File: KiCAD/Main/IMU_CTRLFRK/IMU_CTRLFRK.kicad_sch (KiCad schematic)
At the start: 12 parts, among them U1 BNO085, U2 BME280, U3 VCNL4040M3OE

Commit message: Continue integrating
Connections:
- net +3V3: now also U1.6 (PS0/WAKE)
- net BNO_CLKSELD: now reaches U1.10 (CLKSEL0)
- net BNO_RST: now reaches U1.11 (~{RST})
- net BNO_INT: now reaches U1.14 (~{H_INT})
- net BNO_MOSI: now reaches U1.17 (SA0/H_MOSI)
- net BNO_CS: now reaches U1.18 (~{H_CS})
- net BNO_SCK: now reaches U1.19 (H_SCL/SCK/RX)
- net BNO_MISO: now reaches U1.20 (H_SDA/H_MISO/TX)
- net BNO_BOOT: now reaches R3.2, U1.4 (~{BOOT})
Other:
- note removed: "Microprocessor Interface"
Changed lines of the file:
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@@
 	(generator_version "9.0")
 	(paper "A4")
-	(text "Microprocessor Interface"
-		(exclude_from_sim no)
-		(at 53.086 107.95 90)
-		(effects
-			(font
-				(size 1.905 1.905)
-			)
-		)
-	)
 	(junction
 		(at 218.44 58.42)
@@
 	)
 	(junction
+		(at 116.84 139.7)
+		(diameter 0)
+		(color 0 0 0 0)
+	)
+	(junction
 		(at 213.36 119.38)
 		(diameter 0)
@@
 	(wire
 		(pts
-			(xy 119.38 142.24) (xy 96.52 142.24)
-		)
-		(stroke
-			(width 0)
-			(type default)
-		)
-	)
-	(wire
-		(pts
 			(xy 180.34 121.92) (xy 184.15 121.92)
 		)
@@
 	(wire
 		(pts
-			(xy 119.38 139.7) (xy 114.3 139.7)
-		)
-		(stroke
-			(width 0)
-			(type default)
-		)
-	)
-	(wire
-		(pts
 			(xy 180.34 127) (xy 233.68 127)
 		)
@@
 	(wire
 		(pts
-			(xy 114.3 109.22) (xy 184.15 109.22)
+			(xy 116.84 109.22) (xy 184.15 109.22)
 		)
 		(stroke
@@
 	(wire
 		(pts
-			(xy 114.3 139.7) (xy 114.3 109.22)
+			(xy 116.84 139.7) (xy 116.84 109.22)
 		)
 		(stroke
@@
 	(wire
 		(pts
+			(xy 116.84 139.7) (xy 116.84 142.24)
+		)
+		(stroke
+			(width 0)
+			(type default)
+		)
+	)
+	(wire
+		(pts
 			(xy 57.15 116.84) (xy 93.98 116.84)
 		)
@@
 	(wire
 		(pts
-			(xy 96.52 142.24) (xy 96.52 114.3)
-		)
-		(stroke
-			(width 0)
-			(type default)
-		)
-	)
-	(wire
-		(pts
 			(xy 109.22 129.54) (xy 109.22 101.6)
 		)
@@
 	(wire
 		(pts
+			(xy 116.84 142.24) (xy 119.38 142.24)
+		)
+		(stroke
+			(width 0)
+			(type default)
+		)
+	)
+	(wire
+		(pts
 			(xy 212.09 26.67) (xy 189.23 26.67)
 		)
@@
 	(wire
 		(pts
-			(xy 57.15 114.3) (xy 96.52 114.3)
+			(xy 116.84 139.7) (xy 119.38 139.7)
 		)
 		(stroke
@@
 			(width 0)
 			(type default)
+		)
+	)
+	(hierarchical_label "BNO_CLKSELD"
+		(shape input)
+		(at 57.15 116.84 180)
+		(effects
+			(font
+				(size 1.27 1.27)
+			)
+			(justify right)
+		)
+	)
+	(hierarchical_label "BNO_SCK"
+		(shape input)
+		(at 57.15 104.14 180)
+		(effects
+			(font
+				(size 1.27 1.27)
+			)
+			(justify right)
+		)
+	)
+	(hierarchical_label "BNO_MISO"
+		(shape input)
+		(at 57.15 101.6 180)
+		(effects
+			(font
+				(size 1.27 1.27)
+			)
+			(justify right)
+		)
+	)
+	(hierarchical_label "BNO_MOSI"
+		(shape input)
+		(at 57.15 99.06 180)
+		(effects
+			(font
+				(size 1.27 1.27)
+			)
+			(justify right)
+		)
+	)
+	(hierarchical_label "BNO_CS"
+		(shape input)
+		(at 57.15 119.38 180)
+		(effects
+			(font
+				(size 1.27 1.27)
+			)
+			(justify right)
+		)
+	)
+	(hierarchical_label "BNO_INT"
+		(shape input)
+		(at 57.15 106.68 180)
+		(effects
+			(font
+				(size 1.27 1.27)
+			)
+			(justify right)
+		)
+	)
+	(hierarchical_label "BNO_RST"
+		(shape input)
+		(at 57.15 96.52 180)
+		(effects
+			(font
+				(size 1.27 1.27)
+			)
+			(justify right)
+		)
+	)
+	(hierarchical_label "BNO_BOOT"
+		(shape input)
+		(at 57.15 109.22 180)
+		(effects
+			(font
+				(size 1.27 1.27)
+			)
+			(justify right)
 		)
 	)
@@
 				)
 			)
+			(project "IMU_CTRLFRK"
+				(path "/bbb10697-a5dd-43b8-9c6f-4c5919cf3463/a6ed620d-2e9d-447a-9d61-86e453a954d4"
+					(reference "C4")
+					(unit 1)
+				)
+			)
 		)
 	)
@@
 				)
 			)
+			(project "IMU_CTRLFRK"
+				(path "/bbb10697-a5dd-43b8-9c6f-4c5919cf3463/a6ed620d-2e9d-447a-9d61-86e453a954d4"
+					(reference "U1")
+					(unit 1)
+				)
+			)
 		)
 	)
@@
 				)
 			)
+			(project "IMU_CTRLFRK"
+				(path "/bbb10697-a5dd-43b8-9c6f-4c5919cf3463/a6ed620d-2e9d-447a-9d61-86e453a954d4"
+					(reference "C3")
+					(unit 1)
+				)
+			)
 		)
 	)
@@
 				)
 			)
+			(project "IMU_CTRLFRK"
+				(path "/bbb10697-a5dd-43b8-9c6f-4c5919cf3463/a6ed620d-2e9d-447a-9d61-86e453a954d4"
+					(reference "C1")
+					(unit 1)
+				)
+			)
 		)
 	)
@@
 				)
 			)
+			(project "IMU_CTRLFRK"
+				(path "/bbb10697-a5dd-43b8-9c6f-4c5919cf3463/a6ed620d-2e9d-447a-9d61-86e453a954d4"
+					(reference "R3")
+					(unit 1)
+				)
+			)
 		)
 	)
@@
 				)
 			)
+			(project "IMU_CTRLFRK"
+				(path "/bbb10697-a5dd-43b8-9c6f-4c5919cf3463/a6ed620d-2e9d-447a-9d61-86e453a954d4"
+					(reference "#PWR08")
+					(unit 1)
+				)
+			)
 		)
 	)
@@
 				)
 			)
+			(project "IMU_CTRLFRK"
+				(path "/bbb10697-a5dd-43b8-9c6f-4c5919cf3463/a6ed620d-2e9d-447a-9d61-86e453a954d4"
+					(reference "#PWR06")
+					(unit 1)
+				)
+			)
 		)
 	)
@@
 			(project "IMU_CTRLFRK"
 				(path "/aead792a-4a3a-422e-8f19-9a151b1cac78"
+					(reference "R1")
+					(unit 1)
+				)
+			)
+			(project "IMU_CTRLFRK"
+				(path "/bbb10697-a5dd-43b8-9c6f-4c5919cf3463/a6ed620d-2e9d-447a-9d61-86e453a954d4"
 					(reference "R1")
 					(unit 1)
@@
 				)
 			)
+			(project "IMU_CTRLFRK"
+				(path "/bbb10697-a5dd-43b8-9c6f-4c5919cf3463/a6ed620d-2e9d-447a-9d61-86e453a954d4"
+					(reference "U2")
+					(unit 1)
+				)
+			)
 		)
 	)
@@
 				)
 			)
+			(project "IMU_CTRLFRK"
+				(path "/bbb10697-a5dd-43b8-9c6f-4c5919cf3463/a6ed620d-2e9d-447a-9d61-86e453a954d4"
+					(reference "#PWR011")
+					(unit 1)
+				)
+			)
 		)
 	)
@@
 				)
 			)
+			(project "IMU_CTRLFRK"
+				(path "/bbb10697-a5dd-43b8-9c6f-4c5919cf3463/a6ed620d-2e9d-447a-9d61-86e453a954d4"
+					(reference "#PWR04")
+					(unit 1)
+				)
+			)
 		)
 	)
@@
 				)
 			)
+			(project "IMU_CTRLFRK"
+				(path "/bbb10697-a5dd-43b8-9c6f-4c5919cf3463/a6ed620d-2e9d-447a-9d61-86e453a954d4"
+					(reference "C2")
+					(unit 1)
+				)
+			)
 		)
 	)
@@
 				)
 			)
+			(project "IMU_CTRLFRK"
+				(path "/bbb10697-a5dd-43b8-9c6f-4c5919cf3463/a6ed620d-2e9d-447a-9d61-86e453a954d4"
+					(reference "#PWR03")
+					(unit 1)
+				)
+			)
 		)
 	)
@@
 				)
 			)
+			(project "IMU_CTRLFRK"
+				(path "/bbb10697-a5dd-43b8-9c6f-4c5919cf3463/a6ed620d-2e9d-447a-9d61-86e453a954d4"
+					(reference "C5")
+					(unit 1)
+				)
+			)
 		)
 	)
@@
 				)
 			)
+			(project "IMU_CTRLFRK"
+				(path "/bbb10697-a5dd-43b8-9c6f-4c5919cf3463/a6ed620d-2e9d-447a-9d61-86e453a954d4"
+					(reference "#PWR010")
+					(unit 1)
+				)
+			)
 		)
 	)
@@
 				)
 			)
+			(project "IMU_CTRLFRK"
+				(path "/bbb10697-a5dd-43b8-9c6f-4c5919cf3463/a6ed620d-2e9d-447a-9d61-86e453a954d4"
+					(reference "#PWR05")
+					(unit 1)
+				)
+			)
 		)
 	)
@@
 				)
 			)
+			(project "IMU_CTRLFRK"
+				(path "/bbb10697-a5dd-43b8-9c6f-4c5919cf3463/a6ed620d-2e9d-447a-9d61-86e453a954d4"
+					(reference "#PWR01")
+					(unit 1)
+				)
+			)
 		)
 	)
@@
 				)
 			)
+			(project "IMU_CTRLFRK"
+				(path "/bbb10697-a5dd-43b8-9c6f-4c5919cf3463/a6ed620d-2e9d-447a-9d61-86e453a954d4"
+					(reference "Y1")
+					(unit 1)
+				)
+			)
 		)
 	)
@@
 				)
 			)
+			(project "IMU_CTRLFRK"
+				(path "/bbb10697-a5dd-43b8-9c6f-4c5919cf3463/a6ed620d-2e9d-447a-9d61-86e453a954d4"
+					(reference "#PWR02")
+					(unit 1)
+				)
+			)
 		)
 	)
@@
 				)
 			)
+			(project "IMU_CTRLFRK"
+				(path "/bbb10697-a5dd-43b8-9c6f-4c5919cf3463/a6ed620d-2e9d-447a-9d61-86e453a954d4"
+					(reference "R2")
+					(unit 1)
+				)
+			)
 		)
 	)
@@
 				)
 			)
+			(project "IMU_CTRLFRK"
+				(path "/bbb10697-a5dd-43b8-9c6f-4c5919cf3463/a6ed620d-2e9d-447a-9d61-86e453a954d4"
+					(reference "#PWR07")
+					(unit 1)
+				)
+			)
 		)
 	)
@@
 				)
 			)
+			(project "IMU_CTRLFRK"
+				(path "/bbb10697-a5dd-43b8-9c6f-4c5919cf3463/a6ed620d-2e9d-447a-9d61-86e453a954d4"
+					(reference "#PWR09")
+					(unit 1)
+				)
+			)
 		)
 	)
@@
 				)
 			)
-		)
-	)
-	(sheet_instances
-		(path "/"
-			(page "1")
-		)
-	)
-	(embedded_fonts no)
+			(project "IMU_CTRLFRK"
+				(path "/bbb10697-a5dd-43b8-9c6f-4c5919cf3463/a6ed620d-2e9d-447a-9d61-86e453a954d4"
+					(reference "U3")
+					(unit 1)
+				)
+			)
+		)
+	)
 )

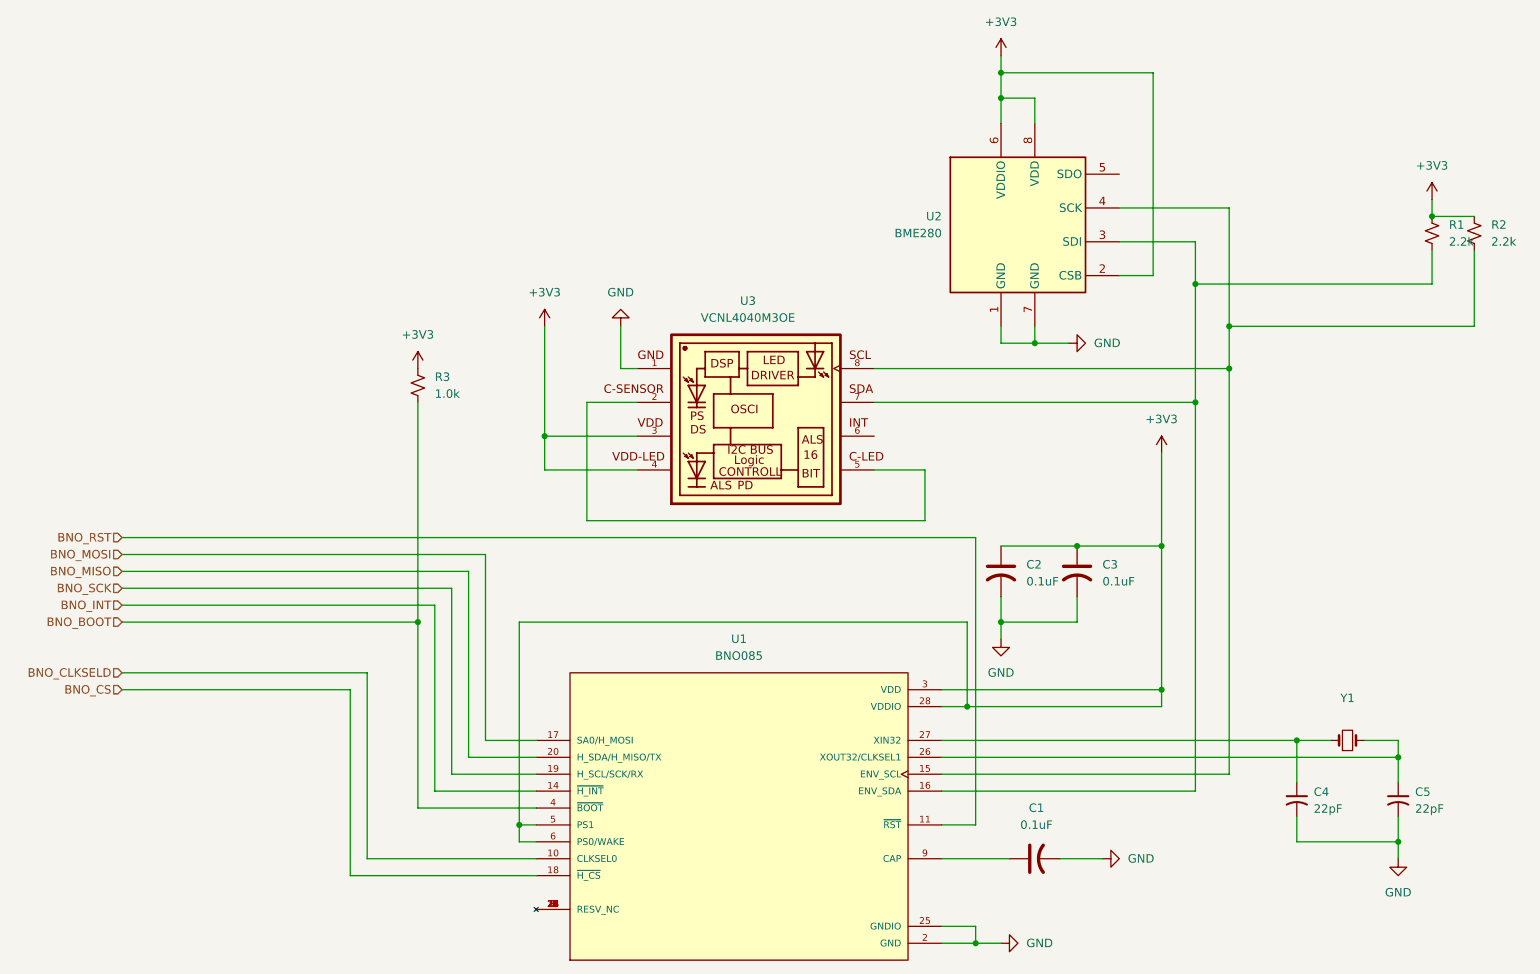
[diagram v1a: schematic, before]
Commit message: Create wiring diagram draft
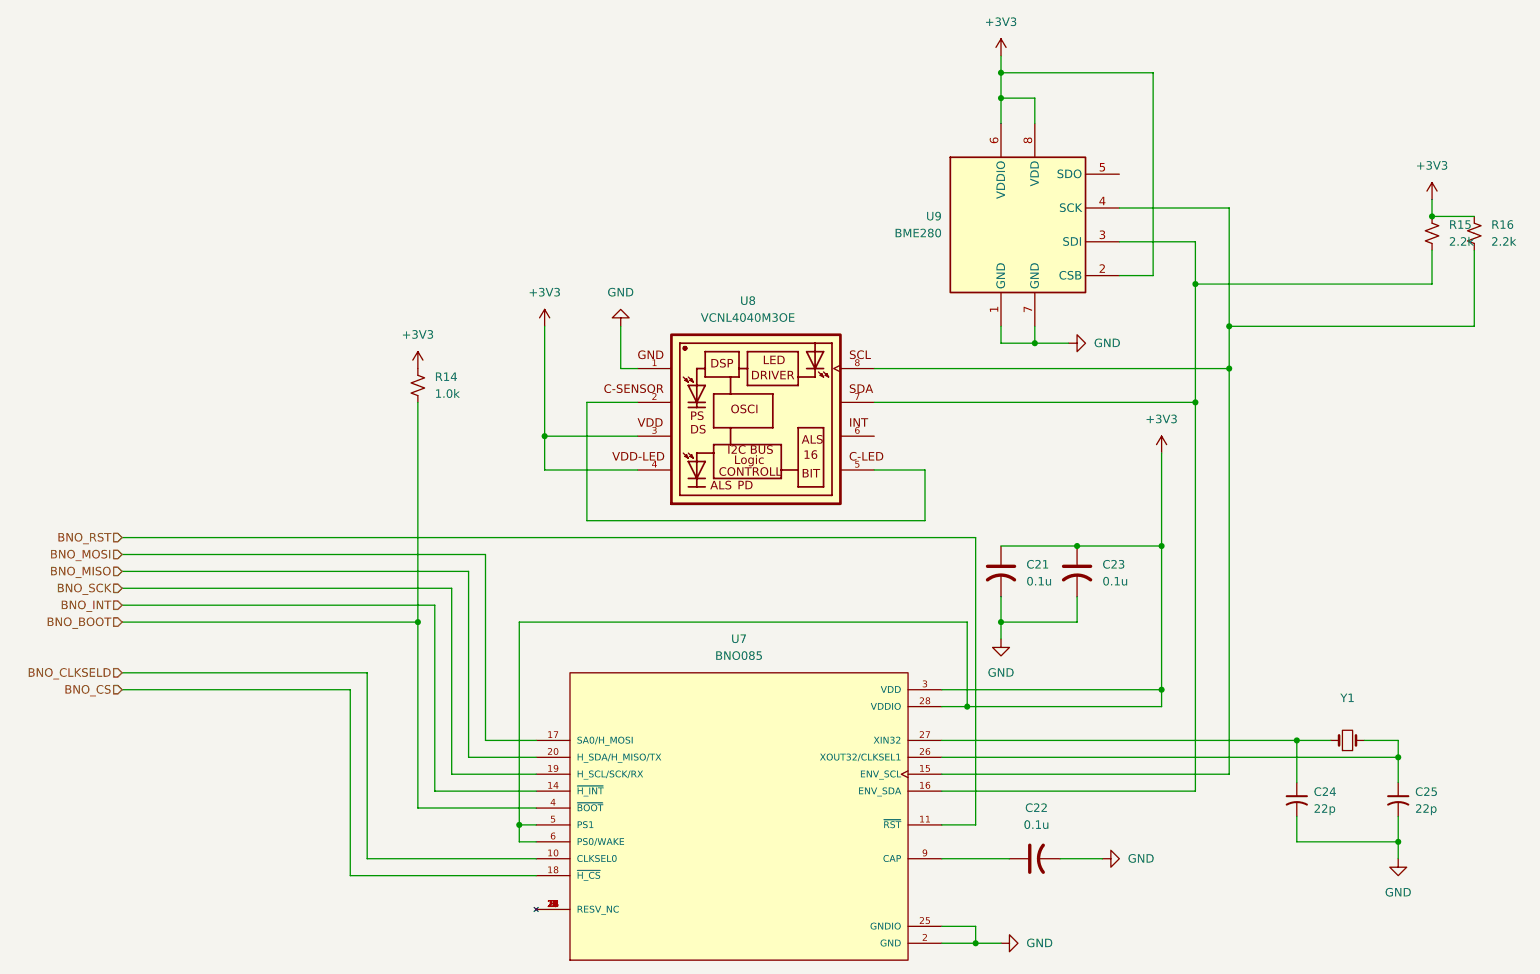
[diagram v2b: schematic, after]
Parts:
- C21: renamed from C2; value 0.1uF -> 0.1u
- C22: renamed from C1; value 0.1uF -> 0.1u
- C23: renamed from C3; value 0.1uF -> 0.1u
- C24: renamed from C4; value 22pF -> 22p
- C25: renamed from C5; value 22pF -> 22p
- renumbered R3 to R14, R1 to R15, R2 to R16, U1 to U7, U3 to U8, U2 to U9
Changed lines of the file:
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@@
 		(dnp no)
 		(fields_autoplaced yes)
-		(property "Reference" "C4"
-			(at 236.22 134.7469 0)
+		(property "Reference" "C24"
+			(at 236.22 134.747 0)
 			(effects
 				(font
@@
 			)
 		)
-		(property "Value" "22pF"
-			(at 236.22 137.2869 0)
+		(property "Value" "22p"
+			(at 236.22 137.287 0)
 			(effects
 				(font
@@
 			(project "IMU_CTRLFRK"
 				(path "/bbb10697-a5dd-43b8-9c6f-4c5919cf3463/a6ed620d-2e9d-447a-9d61-86e453a954d4"
-					(reference "C4")
+					(reference "C24")
 					(unit 1)
 				)
@@
 		(dnp no)
 		(fields_autoplaced yes)
-		(property "Reference" "U1"
+		(property "Reference" "U7"
 			(at 149.86 111.76 0)
 			(effects
@@
 			(project "IMU_CTRLFRK"
 				(path "/bbb10697-a5dd-43b8-9c6f-4c5919cf3463/a6ed620d-2e9d-447a-9d61-86e453a954d4"
-					(reference "U1")
+					(reference "U7")
 					(unit 1)
 				)
@@
 		(dnp no)
 		(fields_autoplaced yes)
-		(property "Reference" "C3"
-			(at 204.47 100.5839 0)
+		(property "Reference" "C23"
+			(at 204.47 100.584 0)
 			(effects
 				(font
@@
 			)
 		)
-		(property "Value" "0.1uF"
-			(at 204.47 103.1239 0)
+		(property "Value" "0.1u"
+			(at 204.47 103.124 0)
 			(effects
 				(font
@@
 			(project "IMU_CTRLFRK"
 				(path "/bbb10697-a5dd-43b8-9c6f-4c5919cf3463/a6ed620d-2e9d-447a-9d61-86e453a954d4"
-					(reference "C3")
+					(reference "C23")
 					(unit 1)
 				)
@@
 		(dnp no)
 		(fields_autoplaced yes)
-		(property "Reference" "C1"
+		(property "Reference" "C22"
 			(at 194.564 137.16 90)
 			(effects
@@
 			)
 		)
-		(property "Value" "0.1uF"
+		(property "Value" "0.1u"
 			(at 194.564 139.7 90)
 			(effects
@@
 			(project "IMU_CTRLFRK"
 				(path "/bbb10697-a5dd-43b8-9c6f-4c5919cf3463/a6ed620d-2e9d-447a-9d61-86e453a954d4"
-					(reference "C1")
+					(reference "C22")
 					(unit 1)
 				)
@@
 		(dnp no)
 		(fields_autoplaced yes)
-		(property "Reference" "R3"
+		(property "Reference" "R14"
 			(at 104.14 72.3899 0)
 			(effects
@@
 			(project "IMU_CTRLFRK"
 				(path "/bbb10697-a5dd-43b8-9c6f-4c5919cf3463/a6ed620d-2e9d-447a-9d61-86e453a954d4"
-					(reference "R3")
+					(reference "R14")
 					(unit 1)
 				)
@@
 		(dnp no)
 		(fields_autoplaced yes)
-		(property "Reference" "#PWR08"
+		(property "Reference" "#PWR040"
 			(at 101.6 74.93 0)
 			(effects
@@
 			(project "IMU_CTRLFRK"
 				(path "/bbb10697-a5dd-43b8-9c6f-4c5919cf3463/a6ed620d-2e9d-447a-9d61-86e453a954d4"
-					(reference "#PWR08")
+					(reference "#PWR040")
 					(unit 1)
 				)
@@
 		(dnp no)
 		(fields_autoplaced yes)
-		(property "Reference" "#PWR06"
+		(property "Reference" "#PWR048"
 			(at 213.36 87.63 0)
 			(effects
@@
 			(project "IMU_CTRLFRK"
 				(path "/bbb10697-a5dd-43b8-9c6f-4c5919cf3463/a6ed620d-2e9d-447a-9d61-86e453a954d4"
-					(reference "#PWR06")
+					(reference "#PWR048")
 					(unit 1)
 				)
@@
 		(on_board yes)
 		(dnp no)
-		(property "Reference" "R1"
+		(property "Reference" "R15"
 			(at 256.54 49.5299 0)
 			(effects
@@
 			(project "IMU_CTRLFRK"
 				(path "/bbb10697-a5dd-43b8-9c6f-4c5919cf3463/a6ed620d-2e9d-447a-9d61-86e453a954d4"
-					(reference "R1")
+					(reference "R15")
 					(unit 1)
 				)
@@
 		(dnp no)
 		(fields_autoplaced yes)
-		(property "Reference" "U2"
+		(property "Reference" "U9"
 			(at 180.34 48.2599 0)
 			(effects
@@
 			(project "IMU_CTRLFRK"
 				(path "/bbb10697-a5dd-43b8-9c6f-4c5919cf3463/a6ed620d-2e9d-447a-9d61-86e453a954d4"
-					(reference "U2")
+					(reference "U9")
 					(unit 1)
 				)
@@
 		(dnp no)
 		(fields_autoplaced yes)
-		(property "Reference" "#PWR011"
+		(property "Reference" "#PWR041"
 			(at 120.65 68.58 0)
 			(effects
@@
 			(project "IMU_CTRLFRK"
 				(path "/bbb10697-a5dd-43b8-9c6f-4c5919cf3463/a6ed620d-2e9d-447a-9d61-86e453a954d4"
-					(reference "#PWR011")
+					(reference "#PWR041")
 					(unit 1)
 				)
@@
 		(dnp no)
 		(fields_autoplaced yes)
-		(property "Reference" "#PWR04"
+		(property "Reference" "#PWR047"
 			(at 210.82 144.78 0)
 			(effects
@@
 			(project "IMU_CTRLFRK"
 				(path "/bbb10697-a5dd-43b8-9c6f-4c5919cf3463/a6ed620d-2e9d-447a-9d61-86e453a954d4"
-					(reference "#PWR04")
+					(reference "#PWR047")
 					(unit 1)
 				)
@@
 		(dnp no)
 		(fields_autoplaced yes)
-		(property "Reference" "C2"
-			(at 193.04 100.5839 0)
+		(property "Reference" "C21"
+			(at 193.04 100.584 0)
 			(effects
 				(font
@@
 			)
 		)
-		(property "Value" "0.1uF"
-			(at 193.04 103.1239 0)
+		(property "Value" "0.1u"
+			(at 193.04 103.124 0)
 			(effects
 				(font
@@
 			(project "IMU_CTRLFRK"
 				(path "/bbb10697-a5dd-43b8-9c6f-4c5919cf3463/a6ed620d-2e9d-447a-9d61-86e453a954d4"
-					(reference "C2")
+					(reference "C21")
 					(unit 1)
 				)
@@
 		(dnp no)
 		(fields_autoplaced yes)
-		(property "Reference" "#PWR03"
+		(property "Reference" "#PWR045"
 			(at 195.58 157.48 0)
 			(effects
@@
 			(project "IMU_CTRLFRK"
 				(path "/bbb10697-a5dd-43b8-9c6f-4c5919cf3463/a6ed620d-2e9d-447a-9d61-86e453a954d4"
-					(reference "#PWR03")
+					(reference "#PWR045")
 					(unit 1)
 				)
@@
 		(dnp no)
 		(fields_autoplaced yes)
-		(property "Reference" "C5"
-			(at 251.46 134.7469 0)
+		(property "Reference" "C25"
+			(at 251.46 134.747 0)
 			(effects
 				(font
@@
 			)
 		)
-		(property "Value" "22pF"
-			(at 251.46 137.2869 0)
+		(property "Value" "22p"
+			(at 251.46 137.287 0)
 			(effects
 				(font
@@
 			(project "IMU_CTRLFRK"
 				(path "/bbb10697-a5dd-43b8-9c6f-4c5919cf3463/a6ed620d-2e9d-447a-9d61-86e453a954d4"
-					(reference "C5")
+					(reference "C25")
 					(unit 1)
 				)
@@
 		(dnp no)
 		(fields_autoplaced yes)
-		(property "Reference" "#PWR010"
+		(property "Reference" "#PWR042"
 			(at 132.08 58.42 0)
 			(effects
@@
 			(project "IMU_CTRLFRK"
 				(path "/bbb10697-a5dd-43b8-9c6f-4c5919cf3463/a6ed620d-2e9d-447a-9d61-86e453a954d4"
-					(reference "#PWR010")
+					(reference "#PWR042")
 					(unit 1)
 				)
@@
 		(dnp no)
 		(fields_autoplaced yes)
-		(property "Reference" "#PWR05"
+		(property "Reference" "#PWR044"
 			(at 189.23 118.11 0)
 			(effects
@@
 			(project "IMU_CTRLFRK"
 				(path "/bbb10697-a5dd-43b8-9c6f-4c5919cf3463/a6ed620d-2e9d-447a-9d61-86e453a954d4"
-					(reference "#PWR05")
+					(reference "#PWR044")
 					(unit 1)
 				)
@@
 		(dnp no)
 		(fields_autoplaced yes)
-		(property "Reference" "#PWR01"
+		(property "Reference" "#PWR046"
 			(at 205.74 67.31 0)
 			(effects
@@
 			(project "IMU_CTRLFRK"
 				(path "/bbb10697-a5dd-43b8-9c6f-4c5919cf3463/a6ed620d-2e9d-447a-9d61-86e453a954d4"
-					(reference "#PWR01")
+					(reference "#PWR046")
 					(unit 1)
 				)
@@
 		(dnp no)
 		(fields_autoplaced yes)
-		(property "Reference" "#PWR02"
+		(property "Reference" "#PWR043"
 			(at 189.23 27.94 0)
 			(effects
@@
 			(project "IMU_CTRLFRK"
 				(path "/bbb10697-a5dd-43b8-9c6f-4c5919cf3463/a6ed620d-2e9d-447a-9d61-86e453a954d4"
-					(reference "#PWR02")
+					(reference "#PWR043")
 					(unit 1)
 				)
@@
 		(dnp no)
 		(fields_autoplaced yes)
-		(property "Reference" "R2"
+		(property "Reference" "R16"
 			(at 262.89 49.5299 0)
 			(effects
@@
 			(project "IMU_CTRLFRK"
 				(path "/bbb10697-a5dd-43b8-9c6f-4c5919cf3463/a6ed620d-2e9d-447a-9d61-86e453a954d4"
-					(reference "R2")
+					(reference "R16")
 					(unit 1)
 				)
@@
 		(dnp no)
 		(fields_autoplaced yes)
-		(property "Reference" "#PWR07"
+		(property "Reference" "#PWR050"
 			(at 254 49.53 0)
 			(effects
@@
 			(project "IMU_CTRLFRK"
 				(path "/bbb10697-a5dd-43b8-9c6f-4c5919cf3463/a6ed620d-2e9d-447a-9d61-86e453a954d4"
-					(reference "#PWR07")
+					(reference "#PWR050")
 					(unit 1)
 				)
@@
 		(dnp no)
 		(fields_autoplaced yes)
-		(property "Reference" "#PWR09"
+		(property "Reference" "#PWR049"
 			(at 248.92 151.13 0)
 			(effects
@@
 			(project "IMU_CTRLFRK"
 				(path "/bbb10697-a5dd-43b8-9c6f-4c5919cf3463/a6ed620d-2e9d-447a-9d61-86e453a954d4"
-					(reference "#PWR09")
+					(reference "#PWR049")
 					(unit 1)
 				)
@@
 		(dnp no)
 		(fields_autoplaced yes)
-		(property "Reference" "U3"
+		(property "Reference" "U8"
 			(at 151.2076 60.96 0)
 			(effects
@@
 			(project "IMU_CTRLFRK"
 				(path "/bbb10697-a5dd-43b8-9c6f-4c5919cf3463/a6ed620d-2e9d-447a-9d61-86e453a954d4"
-					(reference "U3")
-					(unit 1)
-				)
+					(reference "U8")
+					(unit 1)
+				)
